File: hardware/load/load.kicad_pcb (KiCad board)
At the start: 2 copper layers, 107.5 x 120 mm, 135 parts, among them J101 vin_kelvin, J102 uart, J103 panel, J104 external_trigger, J105 input, J106 dut, J107 fan, J108 fuse 20A, J401 temp_sensor, K501 SANYOU_SRD_Form_C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

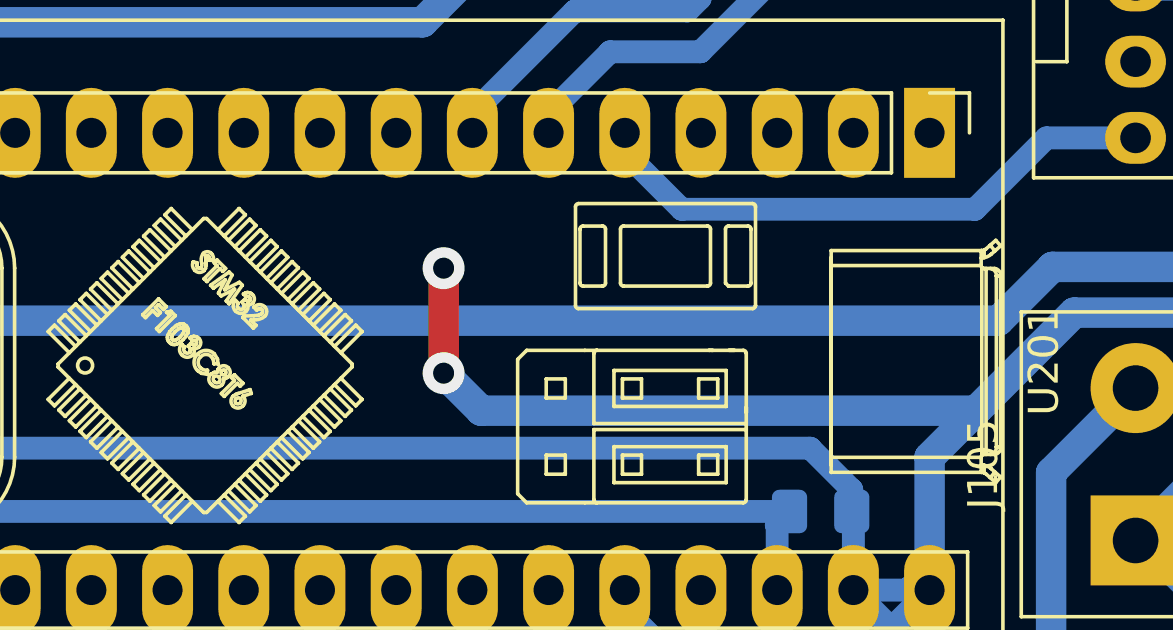
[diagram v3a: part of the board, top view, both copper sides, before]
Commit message: feat(load): modify analog PID values on the schematic
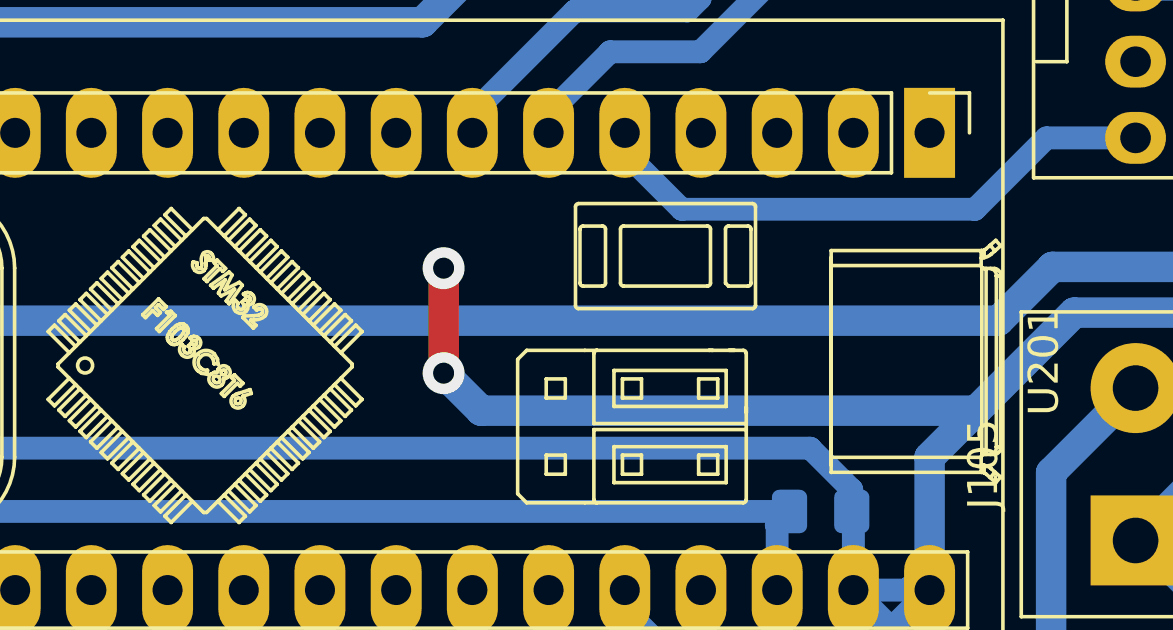
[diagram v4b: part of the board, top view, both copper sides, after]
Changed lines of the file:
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@@
 		(tags "terminal block bornier3")
 		(property "Reference" "Q501"
-			(at 5.05 -4.65 360)
+			(at 5.05 -4.65 0)
 			(layer "F.SilkS")
 			(effects
@@
 		)
 		(property "Value" "2STC4468"
-			(at 5.08 5.08 360)
+			(at 5.08 5.08 0)
 			(layer "F.Fab")
 			(effects
@@
 		)
 		(fp_text user "${REFERENCE}"
-			(at 5.08 0 360)
+			(at 5.08 0 0)
 			(layer "F.Fab")
 			(effects
@@
 		(tags "terminal block bornier3")
 		(property "Reference" "Q504"
-			(at 5.05 -4.65 360)
+			(at 5.05 -4.65 0)
 			(layer "F.SilkS")
 			(effects
@@
 		)
 		(property "Value" "2STC4468"
-			(at 5.08 5.08 360)
+			(at 5.08 5.08 0)
 			(layer "F.Fab")
 			(effects
@@
 		)
 		(fp_text user "${REFERENCE}"
-			(at 5.08 0 360)
+			(at 5.08 0 0)
 			(layer "F.Fab")
 			(effects
@@
 		(fp_arc
 			(start 3.834188 38.743851)
-			(mid 3.811619 38.645125)
+			(mid 3.811624 38.645124)
 			(end 3.8118 38.543851)
 			(stroke
@@
 		(fp_arc
 			(start 7.307593 24.825193)
-			(mid 7.224567 24.861776)
+			(mid 7.22454 24.861815)
 			(end 7.139528 24.83008)
 			(stroke
@@
 		(fp_arc
 			(start 7.409792 24.570015)
-			(mid 7.479426 24.750402)
+			(mid 7.479423 24.750402)
 			(end 7.397576 24.925586)
 			(stroke
@@
 		(fp_arc
 			(start 4.580198 24.492993)
-			(mid 4.448646 24.563813)
+			(mid 4.448637 24.563839)
 			(end 4.300159 24.547174)
 			(stroke
@@
 		(fp_arc
 			(start 6.848655 24.359455)
-			(mid 6.990347 24.294539)
+			(mid 6.990319 24.294578)
 			(end 7.13581 24.350425)
 			(stroke
@@
 		(fp_arc
 			(start 4.017252 24.209874)
-			(mid 3.962123 24.072059)
+			(mid 3.96212 24.072059)
 			(end 4.021927 23.93621)
 			(stroke
@@
 		(fp_arc
 			(start 4.588483 24.182785)
-			(mid 4.651919 24.339695)
+			(mid 4.651922 24.339695)
 			(end 4.580197 24.492993)
 			(stroke
@@
 		(fp_arc
 			(start 4.116052 24.032461)
-			(mid 4.178525 24.004403)
+			(mid 4.178519 24.004429)
 			(end 4.246722 24.010576)
 			(stroke
@@
 		(fp_arc
 			(start 8.143884 23.689744)
-			(mid 8.222175 23.652102)
+			(mid 8.222147 23.65214)
 			(end 8.303556 23.682413)
 			(stroke
@@
 		(fp_arc
 			(start 8.405224 23.593706)
-			(mid 8.472716 23.767948)
+			(mid 8.472713 23.767948)
 			(end 8.388439 23.934723)
 			(stroke
@@
 		(fp_arc
 			(start 7.927268 23.591688)
-			(mid 7.90017 23.534351)
+			(mid 7.900204 23.53435)
 			(end 7.923231 23.475252)
 			(stroke
@@
 		(fp_arc
 			(start 8.042109 23.475359)
-			(mid 8.071049 23.534448)
+			(mid 8.071084 23.534447)
 			(end 8.047421 23.59583)
 			(stroke
@@
 		(fp_arc
 			(start 7.830381 23.377727)
-			(mid 7.98111 23.311522)
+			(mid 7.98111 23.31149)
 			(end 8.132729 23.375603)
 			(stroke
@@
 		(fp_arc
 			(start 8.865971 23.116174)
-			(mid 8.832293 23.047276)
+			(mid 8.832258 23.047276)
 			(end 8.858427 22.9752)
 			(stroke
@@
 		(fp_arc
 			(start 5.845786 23.037029)
-			(mid 5.762735 23.073696)
+			(mid 5.762762 23.073657)
 			(end 5.677721 23.041916)
 			(stroke
@@
 		(fp_arc
 			(start 9.001952 22.980192)
-			(mid 9.035466 23.051001)
+			(mid 9.035428 23.050974)
 			(end 9.008326 23.124461)
 			(stroke
@@
 		(fp_arc
 			(start 5.851842 22.876082)
-			(mid 5.883359 22.957863)
+			(mid 5.883388 22.957863)
 			(end 5.845786 23.037029)
 			(stroke
@@
 		(fp_arc
 			(start 5.674003 22.562261)
-			(mid 5.720753 22.647429)
+			(mid 5.720729 22.647422)
 			(end 5.71416 22.744349)
 			(stroke
@@
 		(fp_arc
 			(start 5.887113 22.2614)
-			(mid 5.957315 22.231578)
+			(mid 5.957315 22.231609)
 			(end 6.027025 22.262569)
 			(stroke
@@
 		(fp_arc
 			(start 5.857533 11.702277)
-			(mid 5.828248 11.772979)
+			(mid 5.828254 11.773014)
 			(end 5.757533 11.802277)
 			(stroke
@@
 		(fp_arc
 			(start 5.107533 11.552277)
-			(mid 5.078248 11.622979)
+			(mid 5.078254 11.623014)
 			(end 5.007533 11.652277)
 			(stroke
@@
 		(fp_arc
 			(start 3.107533 10.902277)
-			(mid 3.136826 10.831558)
+			(mid 3.136832 10.831593)
 			(end 3.207533 10.802277)
 			(stroke
@@
 		(fp_arc
 			(start 5.107533 10.202277)
-			(mid 5.078248 10.272979)
+			(mid 5.078254 10.273014)
 			(end 5.007533 10.302277)
 			(stroke
@@
 		(fp_arc
 			(start 3.107533 7.402277)
-			(mid 3.136826 7.331558)
+			(mid 3.136832 7.331593)
 			(end 3.207533 7.302277)
 			(stroke
@@
 		(fp_arc
 			(start 3.107533 6.052277)
-			(mid 3.136826 5.981558)
+			(mid 3.136832 5.981593)
 			(end 3.207533 5.952277)
 			(stroke
@@
 		(fp_arc
 			(start 2.357533 5.902277)
-			(mid 2.386841 5.831583)
+			(mid 2.386841 5.831587)
 			(end 2.457533 5.802277)
 			(stroke
@@
 		(fp_arc
 			(start 11.070011 -1.724215)
-			(mid 11.102263 -1.900884)
+			(mid 11.102268 -1.900879)
 			(end 11.194857 -2.054759)
 			(stroke
@@
 		(fp_arc
 			(start 11.316427 -1.7285)
-			(mid 11.333055 -1.815275)
+			(mid 11.333049 -1.81528)
 			(end 11.378833 -1.890847)
 			(stroke
@@
 		(fp_arc
 			(start 3.861166 -1.890847)
-			(mid 3.906973 -1.815284)
+			(mid 3.906966 -1.815286)
 			(end 3.923572 -1.7285)
 			(stroke
@@
 		(fp_arc
 			(start 4.045142 -2.054759)
-			(mid 4.137707 -1.900875)
+			(mid 4.137732 -1.900877)
 			(end 4.169988 -1.724215)
 			(stroke
@@
 		(fp_arc
 			(start 10.47 -2.226605)
-			(mid 10.636822 -2.175277)
+			(mid 10.63685 -2.175282)
 			(end 10.719999 -2.021817)
 			(stroke
@@
 		(fp_arc
 			(start 10.47 -2.369999)
-			(mid 10.63682 -2.31867)
+			(mid 10.636848 -2.318676)
 			(end 10.719999 -2.165211)
 			(stroke
